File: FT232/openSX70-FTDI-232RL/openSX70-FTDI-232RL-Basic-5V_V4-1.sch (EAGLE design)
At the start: 19 parts, among them IC1 FT232RQ, J1 687106183722, U1 FT232RLSSOP

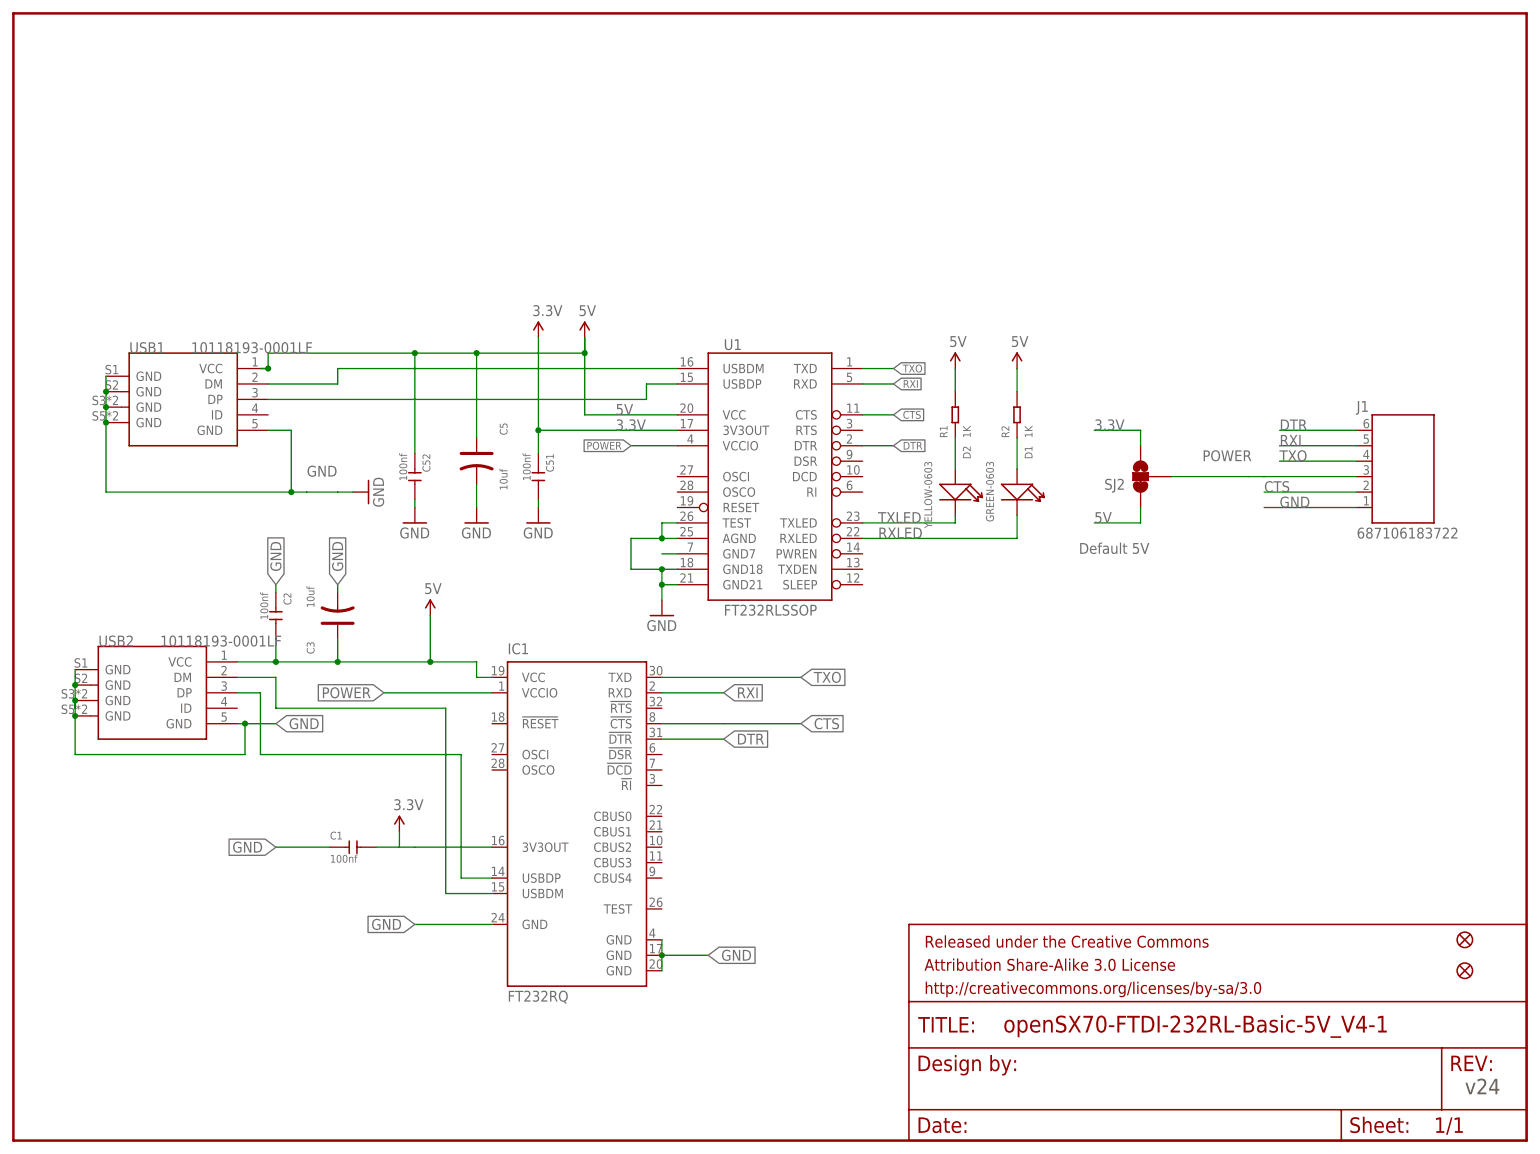
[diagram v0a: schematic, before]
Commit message: New FTDI versions with FT232R L and Q
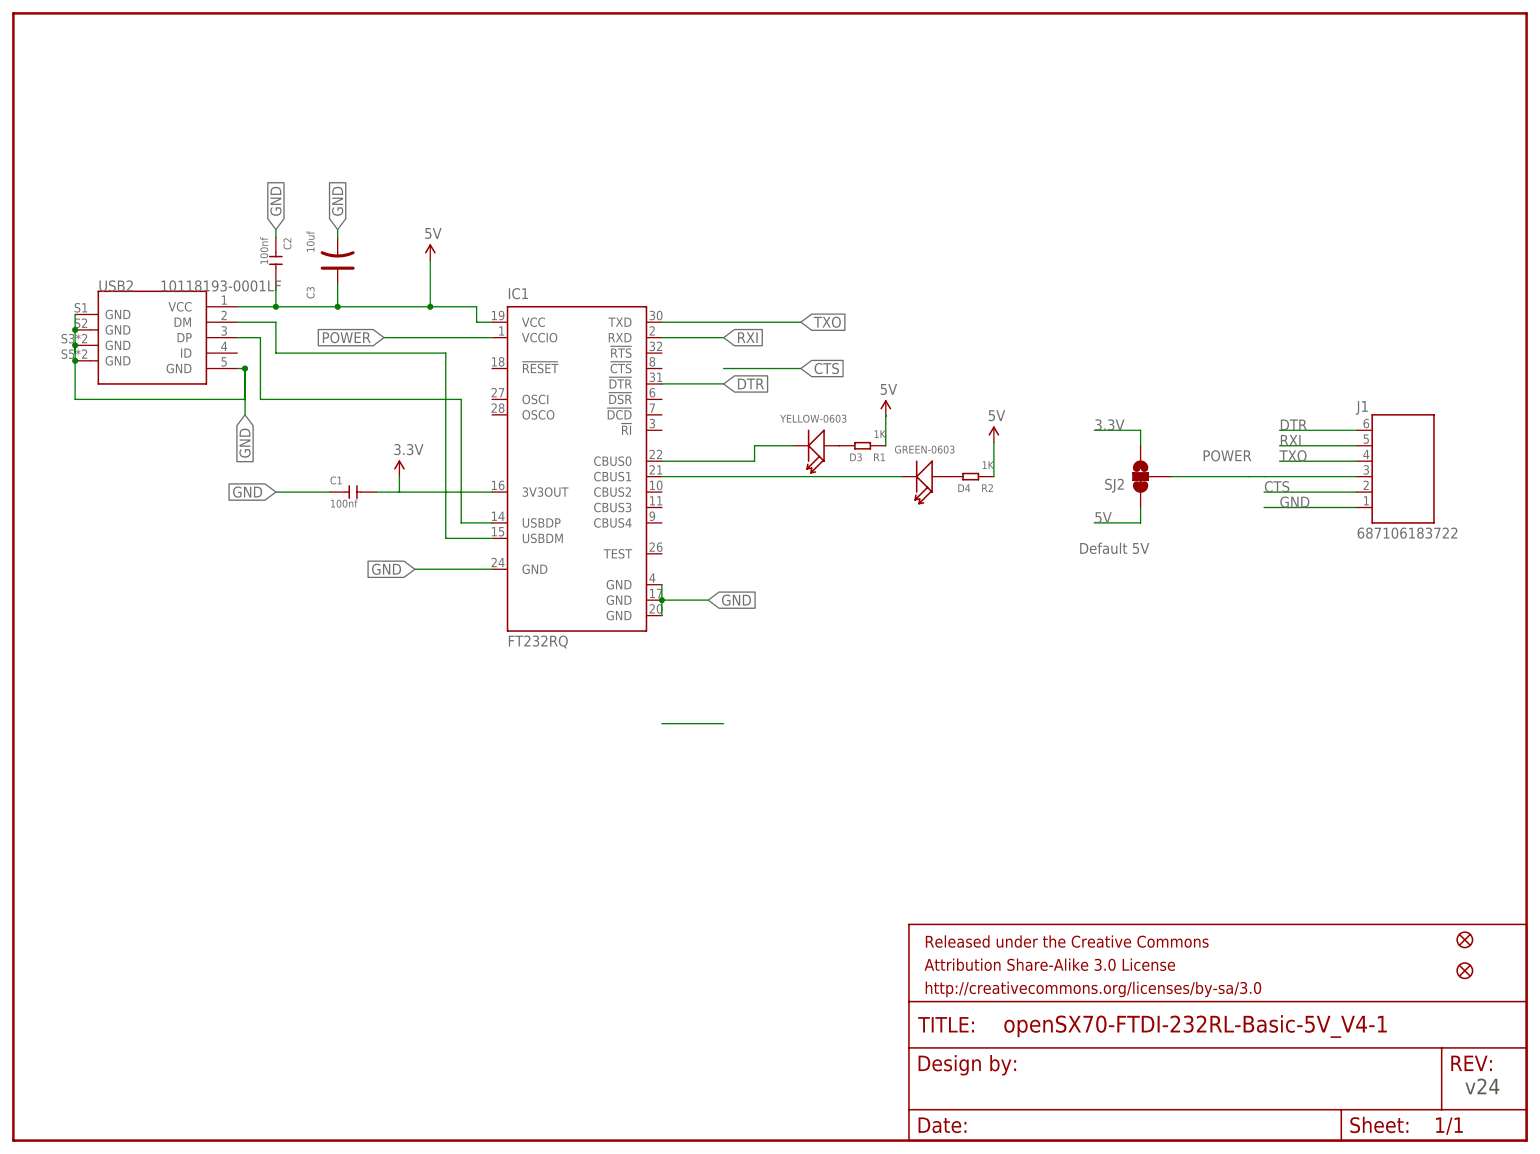
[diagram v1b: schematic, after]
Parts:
- removed C5: 10uf, Seeed-Capacitor-2016:TANTALUM-SMD-10UF-16V-10%(AVX-A)
- removed C51, C52: 100nf, openSX70_PATHFINDER_V5.5-SEEED_20180522:CERAMIC-100NF-50V-10%-X7R(0603)
- removed D1: GREEN-0603, Seeed-LED:SMD-LED-CLEAR-GREEN(0603)
- removed D2: YELLOW-0603, Seeed-LED-2016:SMD-LED-CLEAR-YELLOW(0603)
- removed U1: FT232RLSSOP, SparkFun:FT232RLSSOP
- removed USB1: 10118193-0001LF, Seeed-Connector -2016:MICRO-USB-SMD-B-(10118193-0001LF)
- added D3: YELLOW-0603, Seeed-LED-2016:SMD-LED-CLEAR-YELLOW(0603)
- added D4: GREEN-0603, Seeed-LED:SMD-LED-CLEAR-GREEN(0603)
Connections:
- removed net N$1: D2.+, R1.1
- removed net N$2: D1.+, R2.1
- removed net N$3: U1.USBDM, USB1.DM
- removed net N$5: U1.GND7
- removed net RXLED: D1.-, U1.RXLED
- removed net TXLED: D2.-, U1.TXLED
- removed net USB_D+: U1.USBDP, USB1.DP
- new net N$10: D4.+, R2.2
- new net N$7: D3.-, IC1.CBUS0
- new net N$8: D4.-, IC1.CBUS1
- new net N$9: D3.+, R1.2
- net 3.3V: no longer C51.1, U1.3V3OUT
- net 5V: now also R1.1, R2.1; no longer C5.+, C52.1, R1.2, R2.2, U1.VCC, USB1.VCC
- net CTS: no longer U1.CTS
- net DTR: no longer U1.DTR
- net GND: no longer C5.-, C51.2, C52.2, U1.AGND, U1.GND18, U1.GND21, U1.TEST, USB1.GND@1, USB1.GND@2, USB1.GND@3, USB1.GND@4, USB1.GND@5
- net POWER: no longer U1.VCCIO
- net RXI: no longer U1.RXD
- net TXO: no longer U1.TXD
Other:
- moved on the sheet: C1, C2, C3, IC1, R1, R2, USB2
